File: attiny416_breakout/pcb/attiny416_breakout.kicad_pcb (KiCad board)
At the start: 2 copper layers, 25 x 41.4 mm, 9 parts, among them J1 PROG, J2 5V, J3 GND, J4 Conn_01x10, J5 Conn_01x10, U1 ATtiny416-S

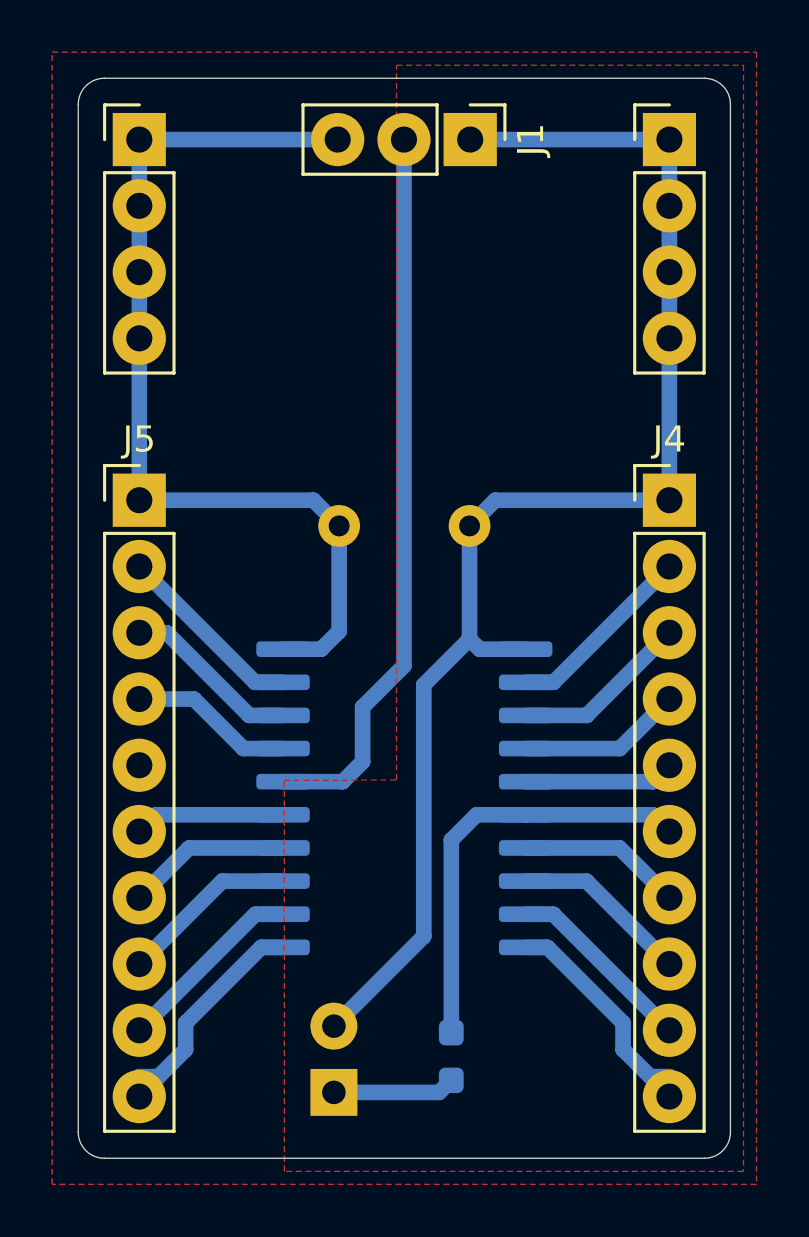
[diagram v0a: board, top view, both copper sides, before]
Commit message: breakout UPDI
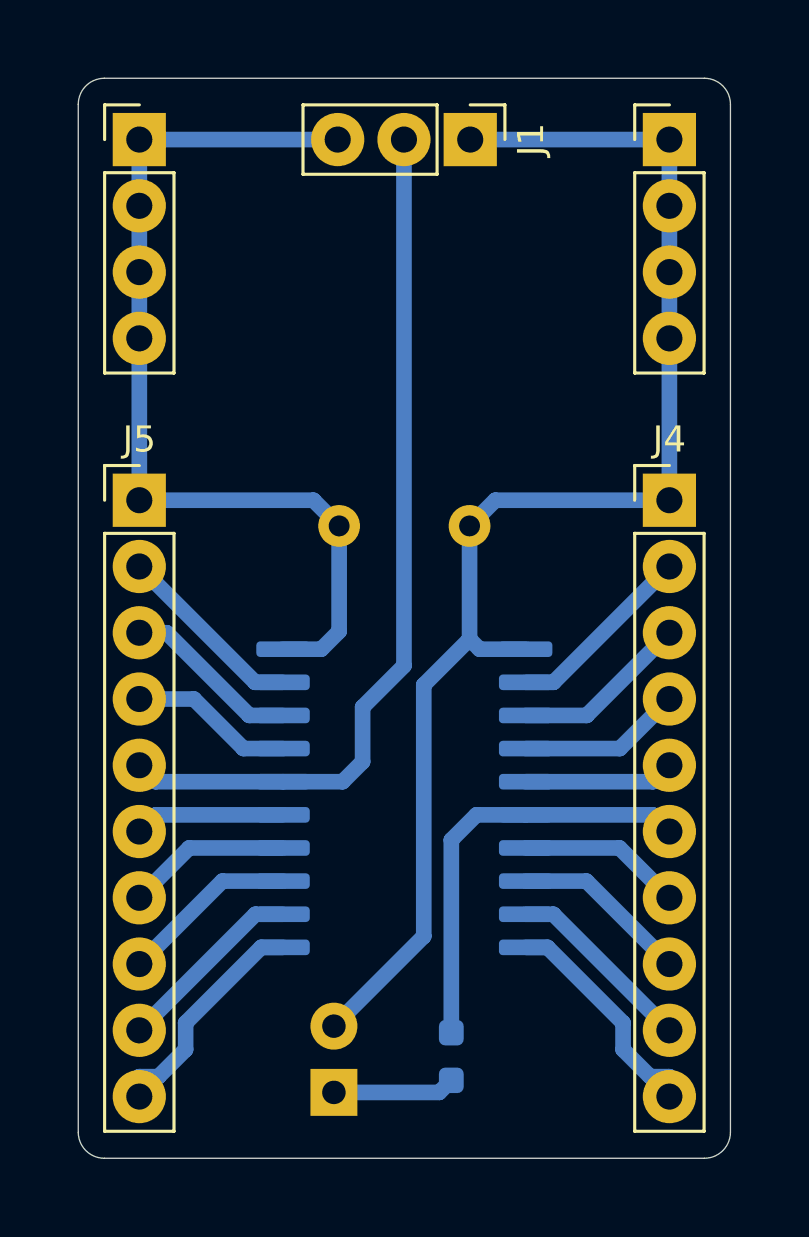
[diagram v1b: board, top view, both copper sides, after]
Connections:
- J5 pad 5: unconnected-(J5-Pin_5-Pad5) -> /UPDI
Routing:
- net /UPDI: track 27.9 -> 33.6 mm
- removed copper zone on F.Cu, net +5V
- removed copper zone on F.Cu, net GND
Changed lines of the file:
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@@
 	(net 14 "/PA3")
 	(net 15 "/PA1")
-	(net 16 "unconnected-(J5-Pin_5-Pad5)")
-	(net 17 "/PC1")
-	(net 18 "/PC0")
-	(net 19 "/PC2")
-	(net 20 "/PB0")
-	(net 21 "/PC3")
-	(net 22 "/PA2")
+	(net 16 "/PC1")
+	(net 17 "/PC0")
+	(net 18 "/PC2")
+	(net 19 "/PB0")
+	(net 20 "/PC3")
+	(net 21 "/PA2")
 	(footprint "pl_mill:PinHeader_1x04_P2.54mm_Vertical"
 		(layer "F.Cu")
@@
 			(layers "*.Cu" "*.Mask")
 			(remove_unused_layers no)
-			(net 22 "/PA2")
+			(net 21 "/PA2")
 			(pinfunction "Pin_3")
 			(pintype "passive")
@@
 			(layers "*.Cu" "*.Mask")
 			(remove_unused_layers no)
-			(net 16 "unconnected-(J5-Pin_5-Pad5)")
+			(net 4 "/UPDI")
 			(pinfunction "Pin_5")
-			(pintype "passive+no_connect")
+			(pintype "passive")
 		)
 		(pad "6" thru_hole oval
@@
 			(layers "*.Cu" "*.Mask")
 			(remove_unused_layers no)
-			(net 21 "/PC3")
+			(net 20 "/PC3")
 			(pinfunction "Pin_6")
 			(pintype "passive")
@@
 			(layers "*.Cu" "*.Mask")
 			(remove_unused_layers no)
-			(net 19 "/PC2")
+			(net 18 "/PC2")
 			(pinfunction "Pin_7")
 			(pintype "passive")
@@
 			(layers "*.Cu" "*.Mask")
 			(remove_unused_layers no)
-			(net 17 "/PC1")
+			(net 16 "/PC1")
 			(pinfunction "Pin_8")
 			(pintype "passive")
@@
 			(layers "*.Cu" "*.Mask")
 			(remove_unused_layers no)
-			(net 18 "/PC0")
+			(net 17 "/PC0")
 			(pinfunction "Pin_9")
 			(pintype "passive")
@@
 			(layers "*.Cu" "*.Mask")
 			(remove_unused_layers no)
-			(net 20 "/PB0")
+			(net 19 "/PB0")
 			(pinfunction "Pin_10")
 			(pintype "passive")
@@
 			(layers "B.Cu" "B.Paste" "B.Mask")
 			(roundrect_rratio 0.25)
-			(net 20 "/PB0")
+			(net 19 "/PB0")
 			(pinfunction "PB0")
 			(pintype "bidirectional")
@@
 			(layers "B.Cu" "B.Paste" "B.Mask")
 			(roundrect_rratio 0.25)
-			(net 18 "/PC0")
+			(net 17 "/PC0")
 			(pinfunction "PC0")
 			(pintype "bidirectional")
@@
 			(layers "B.Cu" "B.Paste" "B.Mask")
 			(roundrect_rratio 0.25)
-			(net 17 "/PC1")
+			(net 16 "/PC1")
 			(pinfunction "PC1")
 			(pintype "bidirectional")
@@
 			(layers "B.Cu" "B.Paste" "B.Mask")
 			(roundrect_rratio 0.25)
-			(net 19 "/PC2")
+			(net 18 "/PC2")
 			(pinfunction "PC2")
 			(pintype "bidirectional")
@@
 			(layers "B.Cu" "B.Paste" "B.Mask")
 			(roundrect_rratio 0.25)
-			(net 21 "/PC3")
+			(net 20 "/PC3")
 			(pinfunction "PC3")
 			(pintype "bidirectional")
@@
 			(layers "B.Cu" "B.Paste" "B.Mask")
 			(roundrect_rratio 0.25)
-			(net 22 "/PA2")
+			(net 21 "/PA2")
 			(pinfunction "PA2")
 			(pintype "bidirectional")
@@
 	)
 	(segment
+		(start 145.35 99.365)
+		(end 140.47 99.365)
+		(width 0.6)
+		(layer "B.Cu")
+		(net 4)
+	)
+	(segment
+		(start 140.47 99.365)
+		(end 139.84 98.735)
+		(width 0.6)
+		(layer "B.Cu")
+		(net 4)
+	)
+	(segment
 		(start 149.985 74.75)
 		(end 149.985 94.92159)
@@
 		(width 0.6)
 		(layer "B.Cu")
-		(net 17)
+		(net 16)
 	)
 	(segment
@@
 		(width 0.6)
 		(layer "B.Cu")
-		(net 17)
+		(net 16)
 	)
 	(segment
@@
 		(width 0.6)
 		(layer "B.Cu")
-		(net 17)
+		(net 16)
 	)
 	(segment
@@
 		(width 0.6)
 		(layer "B.Cu")
-		(net 18)
+		(net 17)
 	)
 	(segment
@@
 		(width 0.6)
 		(layer "B.Cu")
-		(net 18)
+		(net 17)
 	)
 	(segment
@@
 		(width 0.6)
 		(layer "B.Cu")
-		(net 19)
+		(net 18)
 	)
 	(segment
@@
 		(width 0.6)
 		(layer "B.Cu")
-		(net 19)
+		(net 18)
 	)
 	(segment
@@
 		(width 0.6)
 		(layer "B.Cu")
-		(net 20)
+		(net 19)
 	)
 	(segment
@@
 		(width 0.6)
 		(layer "B.Cu")
-		(net 20)
+		(net 19)
 	)
 	(segment
@@
 		(width 0.6)
 		(layer "B.Cu")
-		(net 20)
+		(net 19)
 	)
 	(segment
@@
 		(width 0.6)
 		(layer "B.Cu")
-		(net 20)
+		(net 19)
 	)
 	(segment
@@
 		(width 0.6)
 		(layer "B.Cu")
-		(net 20)
+		(net 19)
 	)
 	(segment
@@
 		(width 0.6)
 		(layer "B.Cu")
-		(net 20)
+		(net 19)
 	)
 	(segment
@@
 		(width 0.6)
 		(layer "B.Cu")
-		(net 21)
+		(net 20)
 	)
 	(segment
@@
 		(width 0.6)
 		(layer "B.Cu")
-		(net 21)
+		(net 20)
 	)
 	(segment
@@
 		(width 0.6)
 		(layer "B.Cu")
-		(net 22)
+		(net 21)
 	)
 	(segment
@@
 		(width 0.6)
 		(layer "B.Cu")
-		(net 22)
+		(net 21)
 	)
 	(segment
@@
 		(width 0.6)
 		(layer "B.Cu")
-		(net 22)
-	)
-	(zone
-		(net 1)
-		(net_name "+5V")
-		(layer "F.Cu")
-		(hatch edge 0.5)
-		(priority 1)
-		(connect_pads
-			(clearance 0.5)
-		)
-		(min_thickness 0.25)
-		(filled_areas_thickness no)
-		(fill yes
-			(thermal_gap 0.5)
-			(thermal_bridge_width 0.5)
-		)
-		(polygon
-			(pts
-				(xy 149.7 71.9) (xy 163 71.9) (xy 163 114.3) (xy 145.4 114.3) (xy 145.4 99.3) (xy 149.7 99.3)
-			)
-		)
-	)
-	(zone
-		(net 2)
-		(net_name "GND")
-		(layer "F.Cu")
-		(hatch edge 0.5)
-		(connect_pads
-			(clearance 0.5)
-		)
-		(min_thickness 0.25)
-		(filled_areas_thickness no)
-		(fill yes
-			(thermal_gap 0.5)
-			(thermal_bridge_width 0.5)
-		)
-		(polygon
-			(pts
-				(xy 136.5 71.4) (xy 163.5 71.4) (xy 163.5 114.8) (xy 136.5 114.8)
-			)
-		)
+		(net 21)
 	)
 )
